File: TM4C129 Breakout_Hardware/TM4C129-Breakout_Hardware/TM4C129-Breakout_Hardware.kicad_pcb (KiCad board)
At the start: 2 copper layers, 47 parts, among them J1 RJ45, J2 Conn_02x08, J3 Conn_02x08, J4 Conn_02x08, J5 Conn_02x02, J6 Conn_02x02, SW1 SW_Push, U1 HX1198FNL, U2 TM4C129ENCPDT, Y1 NX3225GA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

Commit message: started high-level layout
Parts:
- moved R13 116.5 mm to (57.0, 95.8)
- moved J5 107.4 mm to (175.3, 33.0)
- moved J6 102.9 mm to (175.3, 40.6)
- moved C10 100.7 mm to (57.0, 94.0)
- moved C8 97.4 mm to (57.0, 92.2), turned to 180 degrees
- moved C17 93.3 mm to (133.6, 8.38)
- moved C18 89.3 mm to (134.8, 13.7)
- moved C11 87.1 mm to (154.6, 9.91)
- moved C15 82.1 mm to (134.5, 18.3)
- moved C4 81.6 mm to (122.8, 109.5), turned to 180 degrees
- moved C14 81.5 mm to (154.6, 16.5)
- moved C12 79.9 mm to (134.8, 22.9)
- moved R4 77.7 mm to (126.6, 109.5)
- moved C16 77.7 mm to (154.3, 20.6)
- moved R1 77.6 mm to (126.6, 100.6)
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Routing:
- net +3V3: track 0.00 -> 34.6 mm
- net Net-(C8-Pad2): track 0.00 -> 6.35 mm
- net Net-(R8-Pad2): track 0.00 -> 2.92 mm
- net Net-(R7-Pad2): track 0.00 -> 2.92 mm
- net EN0TXO_P: track 0.00 -> 2.54 mm
- net EN0TXO_N: track 0.00 -> 2.54 mm
- net EN0RXI_P: track 0.00 -> 2.54 mm
- net EN0RXI_N: track 0.00 -> 2.54 mm
- net Net-(C9-Pad2): track 0.00 -> 2.39 mm
- net Net-(C7-Pad2): track 0.00 -> 2.26 mm
- net Net-(C10-Pad2): track 0.00 -> 1.78 mm
- added copper zone on F.Cu, net GND
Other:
- net class Default: clearance 0.2 -> 0.1524
- rule trace_clearance: 0.2 -> 0.1524

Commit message: Ran TIVA Traces
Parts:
- moved C10 80.3 mm to (133.2, 119.4)
- moved C8 80.3 mm to (133.2, 117.6)
- moved R13 80.3 mm to (133.2, 121.2)
- moved J5 43.2 mm to (132.1, 33.0)
- moved Conn1 33.1 mm to (180.3, 12.7)
- moved R16 31.4 mm to (138.6, 102.1), turned to 180 degrees
- moved R10 27.2 mm to (138.6, 107.2), turned to 180 degrees
- moved R9 25.6 mm to (138.6, 109.7), turned to 0 degrees
- moved C5 25.5 mm to (156.8, 48.0)
- moved R6 25.5 mm to (156.8, 46.2)
- moved R5 25.5 mm to (156.9, 49.8)
- moved R17 23.7 mm to (138.6, 114.8), turned to 180 degrees
- moved J6 22.7 mm to (154.9, 30.5)
- moved C9 22.0 mm to (151.4, 51.7), turned to 180 degrees
- moved R15 17.8 mm to (150.4, 47.4)
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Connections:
- net Net-(C13-Pad2) renamed /VBAT
- net Net-(C5-Pad2) renamed /RST_In
- net Net-(C6-Pad2) renamed /OSC0
- net Net-(C7-Pad2) renamed /XOSC1
- net Net-(C9-Pad2) renamed /XOSC0
- net Net-(R11-Pad2) renamed /OSC1
- net Net-(R12-Pad2) renamed /RBIAS
- net Net-(R14-Pad2) renamed /Wake
- J6 pad 3: Net-(J6-Pad3) -> +3V3
- J6 pad 4: Net-(J6-Pad4) -> GND
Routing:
- net GND: track 0.00 -> 28.0 mm, vias 0 -> 7
- net RX7: track 0.00 -> 9.54 mm
- net TX7: track 0.00 -> 9.16 mm
- net RX5: track 0.00 -> 8.79 mm
- net TX5: track 0.00 -> 8.41 mm
- net PWM1: track 0.00 -> 8.26 mm
- net PWM2: track 0.00 -> 7.89 mm
- net TX4: track 0.00 -> 7.70 mm
- net PWM3: track 0.00 -> 7.51 mm
- net RX4: track 0.00 -> 7.33 mm
- net Ethernet_Activity: track 0.00 -> 7.13 mm
- net A3: track 0.00 -> 6.62 mm
- net PWM4: track 0.00 -> 6.43 mm
- net T2_A: track 0.00 -> 6.37 mm
- net RX6: track 0.00 -> 6.36 mm
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- added copper zone on F.Cu, net +3V3
- added copper zone on B.Cu, net GND
- removed copper zone on F.Cu, net GND

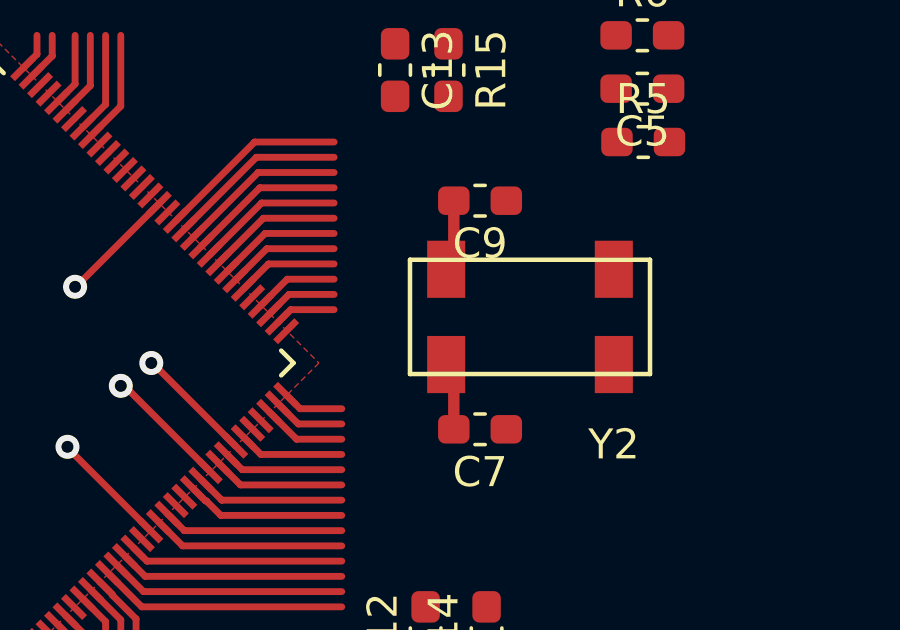
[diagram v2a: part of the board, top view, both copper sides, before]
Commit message: Cleaned up Schematic
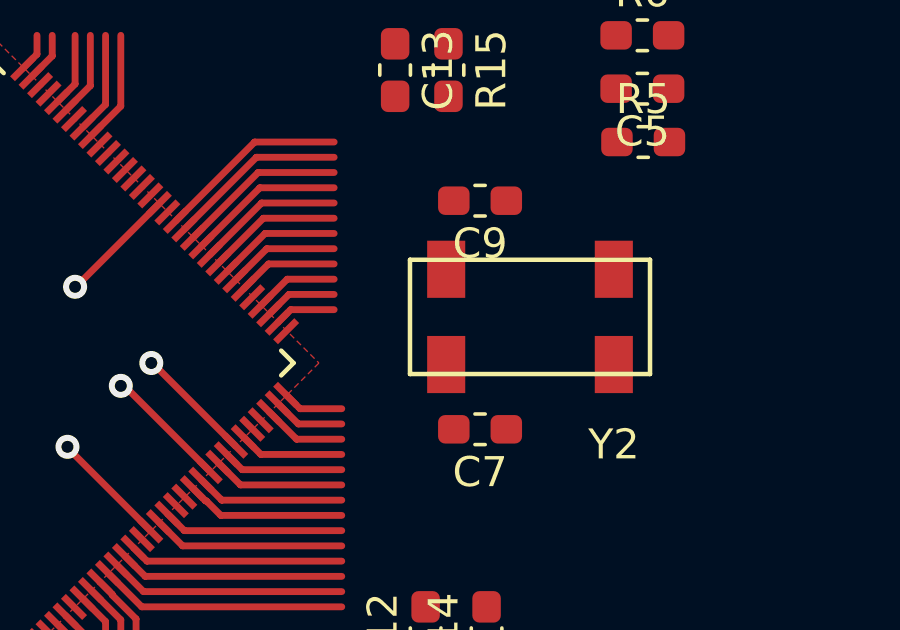
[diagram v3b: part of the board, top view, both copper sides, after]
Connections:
- R11 pad 1: Net-(R11-Pad1) -> /OSC1
- R11 pad 2: /OSC1 -> Net-(R11-Pad2)
- U2 pad 89: Net-(R11-Pad1) -> /OSC1
- Y1 pad 1: /OSC1 -> /OSC0
- Y1 pad 3: /OSC0 -> Net-(R11-Pad2)
- Y2 pad 1: /XOSC1 -> /XOSC0
- Y2 pad 2: /XOSC0 -> /XOSC1
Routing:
- net Net-(R11-Pad1): track 3.39 -> 0.00 mm
- net /OSC1: track 0.00 -> 3.39 mm
- net /XOSC0: track 4.46 -> 2.06 mm
- net /XOSC1: track 4.70 -> 2.44 mm
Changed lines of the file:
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@@
     (thickness 1.6)
     (drawings 2)
-    (tracks 187)
+    (tracks 183)
     (zones 0)
     (modules 47)
@@
     (solder_mask_min_width 0.25)
     (aux_axis_origin 0 0)
-    (visible_elements 7FFFF7FF)
+    (visible_elements 7FFFFFFF)
     (pcbplotparams
       (layerselection 0x010fc_ffffffff)
@@
   (net 76 "Net-(R7-Pad2)")
   (net 77 "Net-(R8-Pad2)")
-  (net 78 "Net-(R11-Pad1)")
+  (net 78 "Net-(R11-Pad2)")
   (net 79 "Net-(U2-Pad5)")
   (net 80 "Net-(U2-Pad6)")
@@
     (add_net "Net-(J1-Pad9)")
     (add_net "Net-(J4-Pad1)")
-    (add_net "Net-(R11-Pad1)")
+    (add_net "Net-(R11-Pad2)")
     (add_net "Net-(R7-Pad2)")
     (add_net "Net-(R8-Pad2)")
@@
       (net 118 /OSC0))
     (pad 89 smd rect (at 7.7 -3.4 45) (size 1 0.23) (layers F.Cu F.Paste F.Mask)
-      (net 78 "Net-(R11-Pad1)"))
+      (net 122 /OSC1))
     (pad 90 smd rect (at 7.7 -3.8 45) (size 1 0.23) (layers F.Cu F.Paste F.Mask)
       (net 2 +3V3))
@@
       (net 116 "Net-(Y1-Pad4)"))
     (pad 3 smd rect (at 1.1078 -0.838) (size 1.4 1.2) (layers F.Cu F.Paste F.Mask)
-      (net 118 /OSC0))
+      (net 78 "Net-(R11-Pad2)"))
     (pad 2 smd rect (at 1.1078 0.762) (size 1.4 1.2) (layers F.Cu F.Paste F.Mask)
       (net 115 "Net-(Y1-Pad2)"))
     (pad 1 smd rect (at -1.0922 0.762) (size 1.4 1.2) (layers F.Cu F.Paste F.Mask)
-      (net 122 /OSC1))
+      (net 118 /OSC0))
   )
   (module MRDT_Devices:ABS25 (layer F.Cu)
@@
     (pad "" smd rect (at 2.794 1.651) (size 1.27 1.905) (layers F.Cu F.Paste F.Mask))
     (pad 1 smd rect (at -2.794 1.651) (size 1.27 1.905) (layers F.Cu F.Paste F.Mask)
-      (net 119 /XOSC1))
+      (net 120 /XOSC0))
     (pad "" smd rect (at 2.794 -1.524) (size 1.27 1.905) (layers F.Cu F.Paste F.Mask))
     (pad 2 smd rect (at -2.794 -1.524) (size 1.27 1.905) (layers F.Cu F.Paste F.Mask)
-      (net 120 /XOSC0))
+      (net 119 /XOSC1))
   )
   (module Capacitor_SMD:C_0603_1608Metric_Pad1.05x0.95mm_HandSolder (layer F.Cu)
@@
     (fp_line (start -0.8 0.4) (end -0.8 -0.4) (layer F.Fab) (width 0.1))
     (pad 2 smd roundrect (at 0.875 0 270) (size 1.05 0.95) (layers F.Cu F.Paste F.Mask) (roundrect_rratio 0.25)
+      (net 78 "Net-(R11-Pad2)"))
+    (pad 1 smd roundrect (at -0.875 0 270) (size 1.05 0.95) (layers F.Cu F.Paste F.Mask) (roundrect_rratio 0.25)
       (net 122 /OSC1))
-    (pad 1 smd roundrect (at -0.875 0 270) (size 1.05 0.95) (layers F.Cu F.Paste F.Mask) (roundrect_rratio 0.25)
-      (net 78 "Net-(R11-Pad1)"))
     (model ${KISYS3DMOD}/Resistor_SMD.3dshapes/R_0603_1608Metric.wrl
       (at (xyz 0 0 0))
@@
   (segment (start 113.538 103.632) (end 115.598 103.632) (width 0.381) (layer F.Cu) (net 2))
   (segment (start 115.598 109.982) (end 115.598 106.172) (width 0.381) (layer F.Cu) (net 2))
-  (segment (start 150.5458 57.4548) (end 150.2918 57.2008) (width 0.381) (layer F.Cu) (net 119))
-  (segment (start 150.5458 59.3598) (end 150.5458 57.4548) (width 0.381) (layer F.Cu) (net 119))
   (segment (start 133.068 104.902) (end 133.068 111.252) (width 0.381) (layer F.Cu) (net 3))
   (segment (start 134.112 119.38) (end 134.112 121.158) (width 0.381) (layer F.Cu) (net 4))
@@
   (segment (start 137.602874 48.735429) (end 138.43 47.908303) (width 0.2286) (layer F.Cu) (net 70))
   (segment (start 138.43 47.908303) (end 138.43 46.228) (width 0.2286) (layer F.Cu) (net 70))
-  (segment (start 150.5458 53.7718) (end 150.2918 54.0258) (width 0.381) (layer F.Cu) (net 120))
-  (segment (start 150.5458 51.7398) (end 150.5458 53.7718) (width 0.381) (layer F.Cu) (net 120))
   (segment (start 117.348 103.632) (end 119.888 103.632) (width 0.381) (layer F.Cu) (net 71))
   (segment (start 142.296635 61.746193) (end 142.780442 62.23) (width 0.2286) (layer F.Cu) (net 71))
@@
   (segment (start 128.397 104.902) (end 131.318 104.902) (width 0.381) (layer F.Cu) (net 76))
   (segment (start 128.397 111.252) (end 131.318 111.252) (width 0.381) (layer F.Cu) (net 77))
-  (segment (start 138.168559 49.301115) (end 138.938 48.531674) (width 0.2286) (layer F.Cu) (net 78))
-  (segment (start 138.938 48.531674) (end 138.938 46.228) (width 0.2286) (layer F.Cu) (net 78))
+  (segment (start 138.168559 49.301115) (end 138.938 48.531674) (width 0.2286) (layer F.Cu) (net 122))
+  (segment (start 138.938 48.531674) (end 138.938 46.228) (width 0.2286) (layer F.Cu) (net 122))
   (segment (start 143.542571 54.675126) (end 144.369697 53.848) (width 0.2286) (layer F.Cu) (net 117))
   (segment (start 144.369697 53.848) (end 146.558 53.848) (width 0.2286) (layer F.Cu) (net 117))

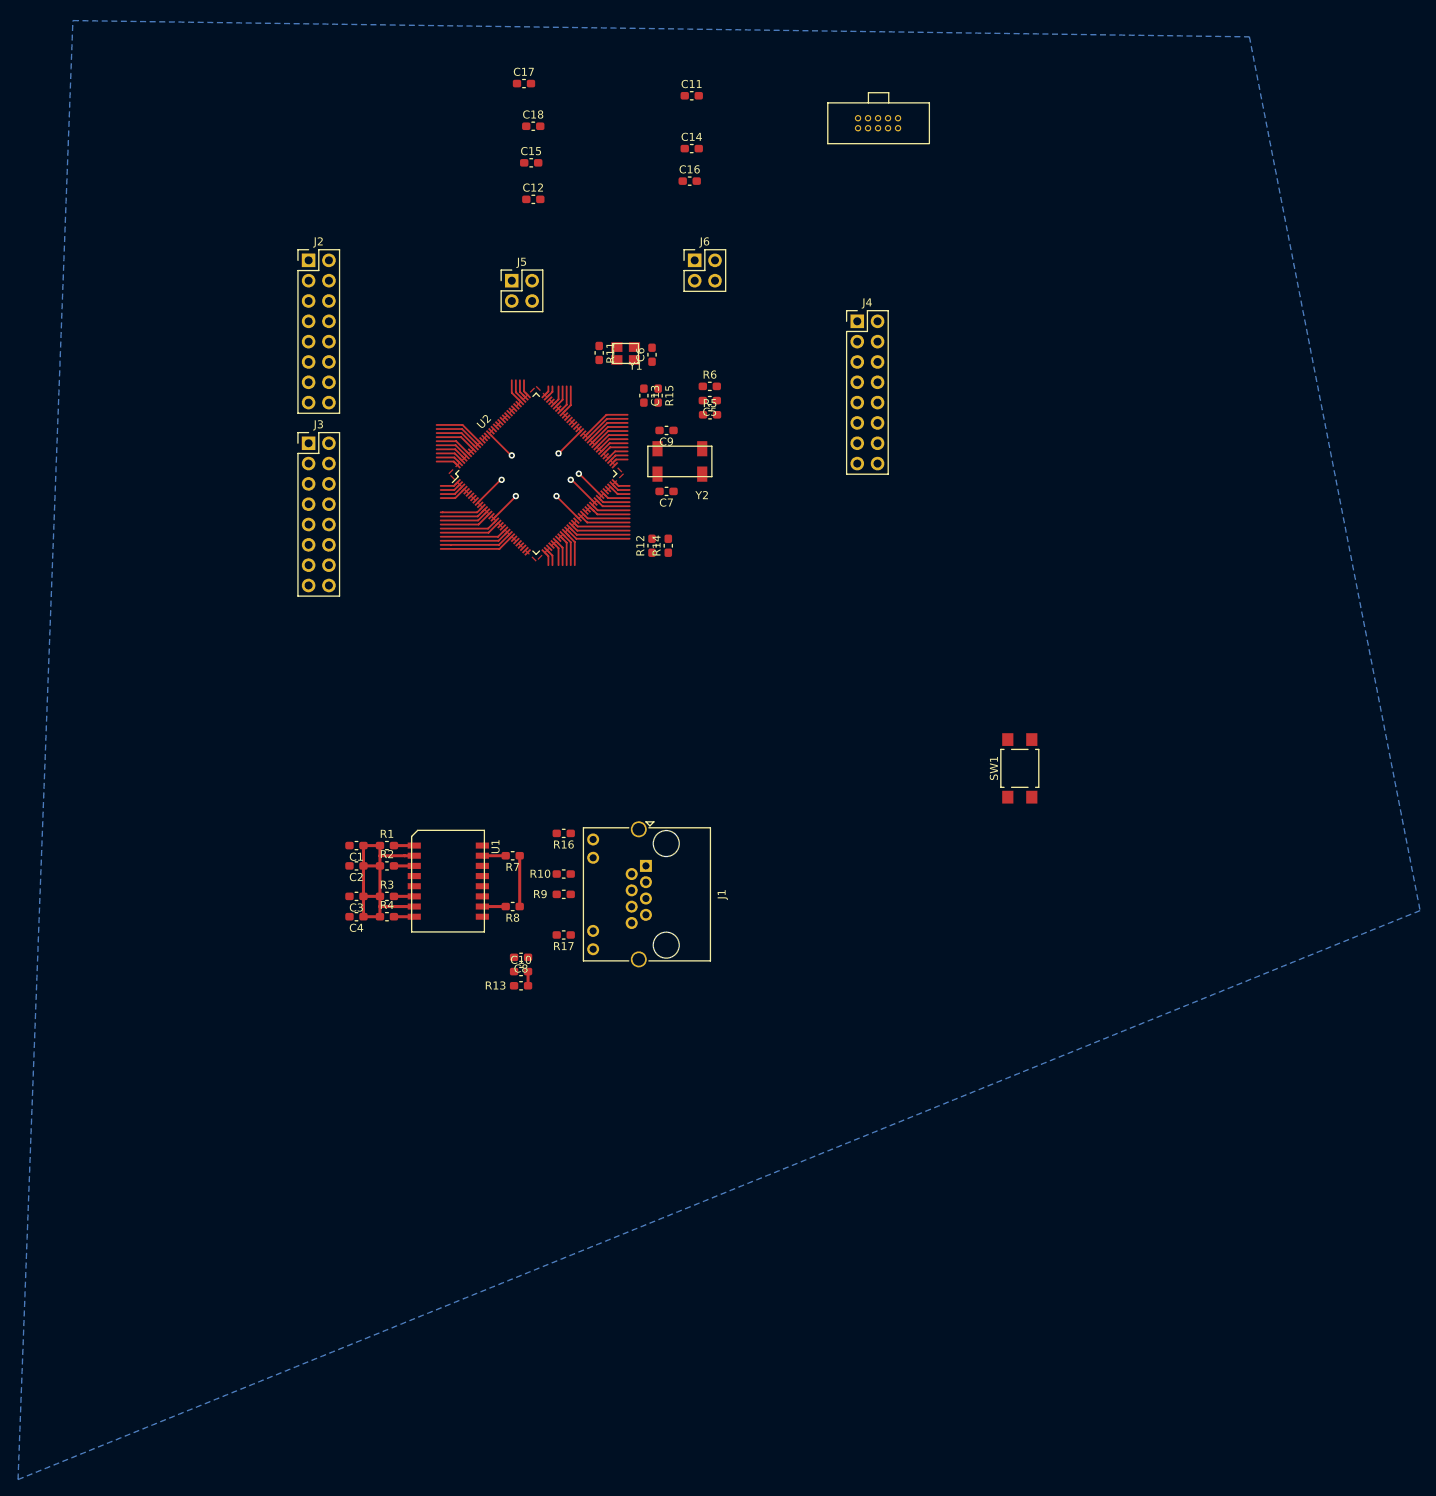
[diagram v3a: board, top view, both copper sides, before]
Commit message: Wired left half traces
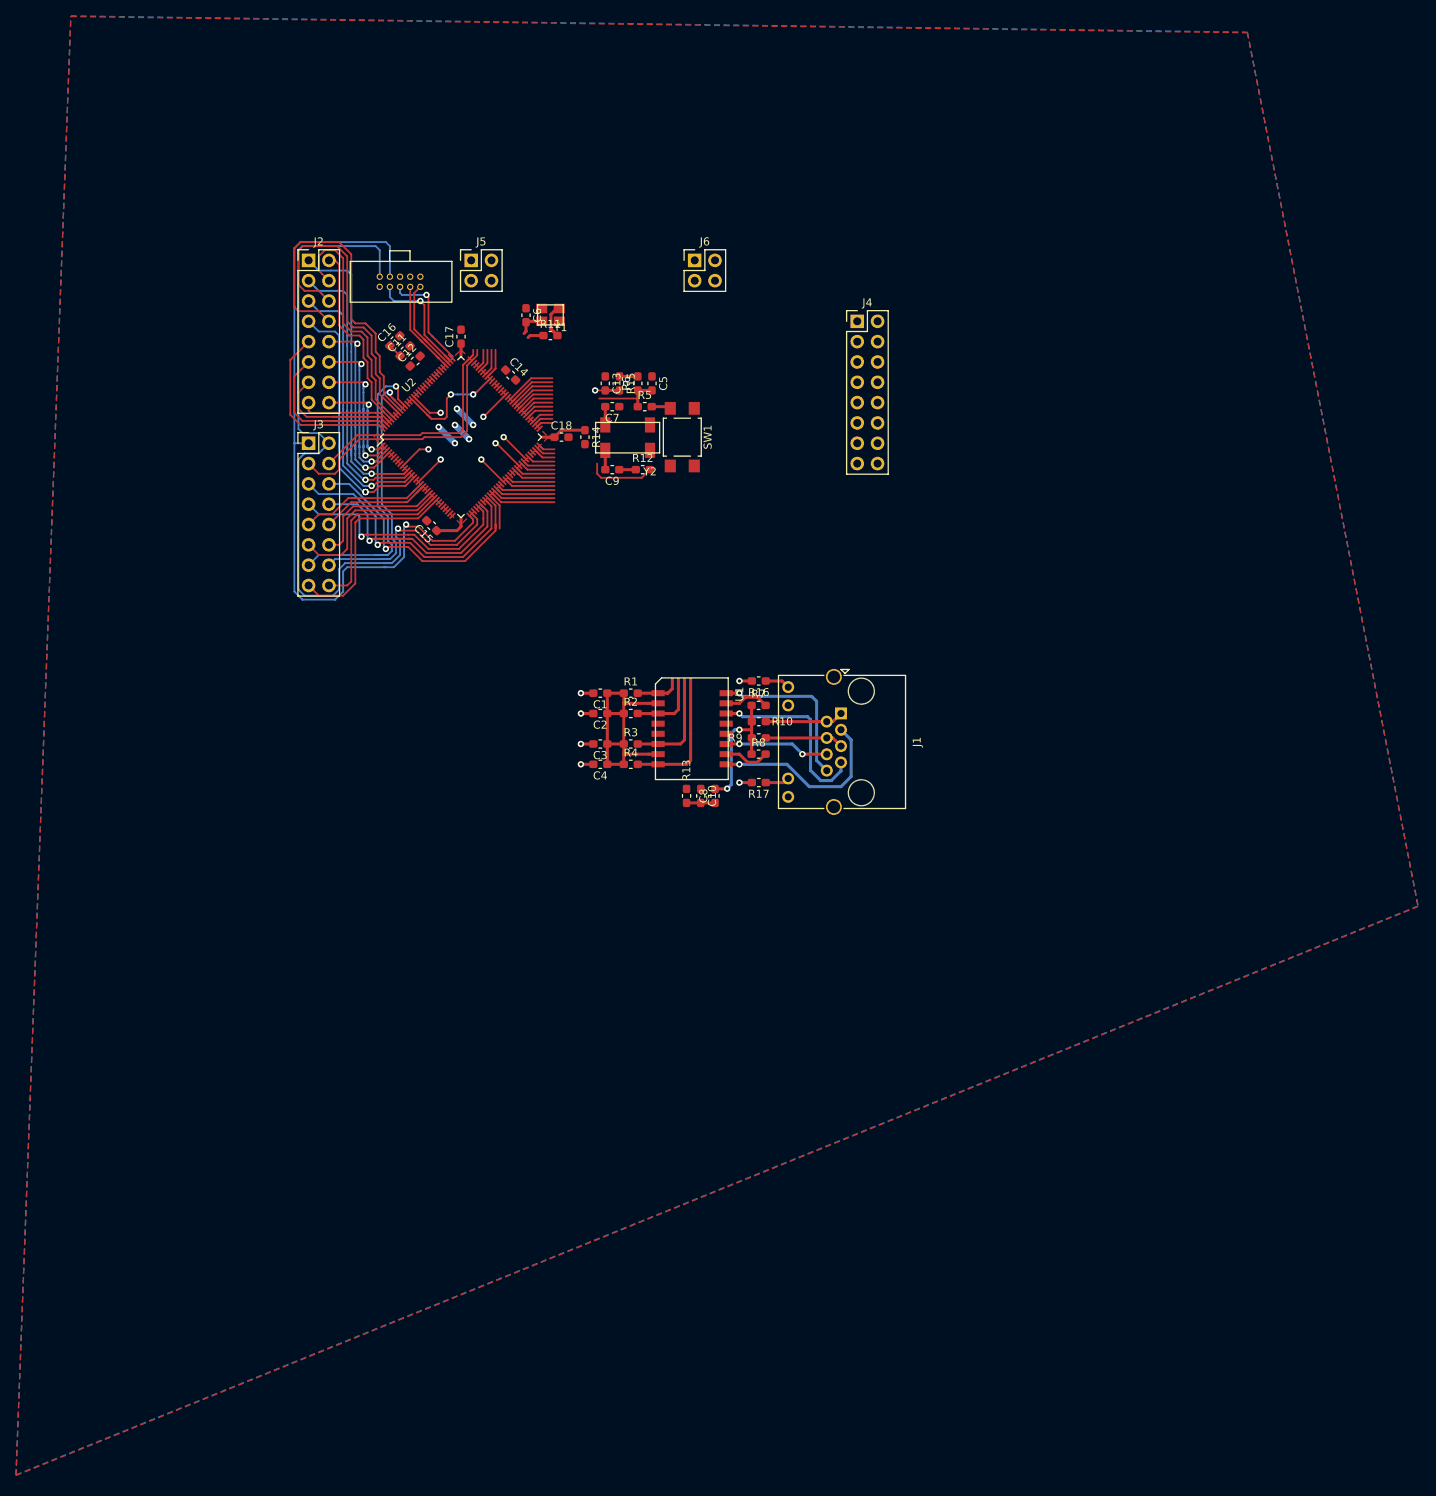
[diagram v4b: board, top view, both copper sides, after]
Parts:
- moved Conn1 62.9 mm to (120.7, 32.5)
- moved SW1 59.1 mm to (153.4, 52.6), turned to 270 degrees
- moved C11 48.0 mm to (118.7, 41.8), turned to 45 degrees
- moved C15 47.0 mm to (122.1, 63.6), turned to 135 degrees
- moved C16 41.9 mm to (117.5, 40.5), turned to 45 degrees
- moved C18 39.0 mm to (138.3, 52.6)
- moved C14 36.2 mm to (131.9, 44.8), turned to 315 degrees
- moved R8 36.2 mm to (162.9, 92.2), turned to 0 degrees
- moved R7 36.0 mm to (162.9, 86.1), turned to 0 degrees
- moved C1 35.9 mm to (143.1, 84.6)
- moved C4 35.9 mm to (143.1, 93.5)
- moved R1 35.9 mm to (147.0, 84.6)
- moved R4 35.9 mm to (147.0, 93.5)
- moved C2 35.9 mm to (143.1, 87.1)
- moved C3 35.9 mm to (143.1, 90.9)
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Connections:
- J3 pad 1: TX0 -> RX0
- J3 pad 10: RX4 -> TX4
- J3 pad 11: TX5 -> RX5
- J3 pad 12: RX5 -> TX5
- J3 pad 13: TX6 -> RX6
- J3 pad 14: RX6 -> TX6
- J3 pad 15: TX7 -> RX7
- J3 pad 16: RX7 -> TX7
- J3 pad 2: RX0 -> TX0
- J3 pad 3: TX1 -> RX1
- J3 pad 4: RX1 -> TX1
- J3 pad 5: TX2 -> RX2
- J3 pad 6: RX2 -> TX2
- J3 pad 7: TX3 -> RX3
- J3 pad 8: RX3 -> TX3
- J3 pad 9: TX4 -> RX4
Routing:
- net TX0: track 2.17 -> 95.9 mm, vias 0 -> 1
- net RX0: track 1.79 -> 95.2 mm, vias 0 -> 1
- net A11: track 5.61 -> 43.3 mm
- net A10: track 5.23 -> 39.0 mm
- net A0: track 5.49 -> 38.5 mm, vias 0 -> 1
- net RX1: track 1.66 -> 34.0 mm
- net RX6: track 6.36 -> 38.3 mm, vias 0 -> 1
- net A1: track 5.87 -> 36.4 mm, vias 0 -> 1
- net RX2: track 3.90 -> 34.2 mm, vias 0 -> 1
- net TX3: track 3.36 -> 32.9 mm, vias 0 -> 1
- net TX2: track 4.28 -> 33.7 mm, vias 0 -> 1
- net A2: track 6.24 -> 35.1 mm, vias 0 -> 1
- net TX6: track 5.98 -> 34.5 mm, vias 0 -> 1
- net TX1: track 1.29 -> 29.0 mm
- net RX3: track 2.98 -> 29.4 mm, vias 0 -> 1
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- added copper zone on F.Cu, net GND
